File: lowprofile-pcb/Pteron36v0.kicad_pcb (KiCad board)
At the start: 2 copper layers, 123.5 x 95.6 mm, 47 parts, among them J1 AudioJack4, J2 AudioJack4, SW1 SW_PUSH, SW10 SW_PUSH, SW12 SW_PUSH, SW13 SW_PUSH, SW14 SW_PUSH, SW15 SW_PUSH, SW17 SW_PUSH, SW18 SW_PUSH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

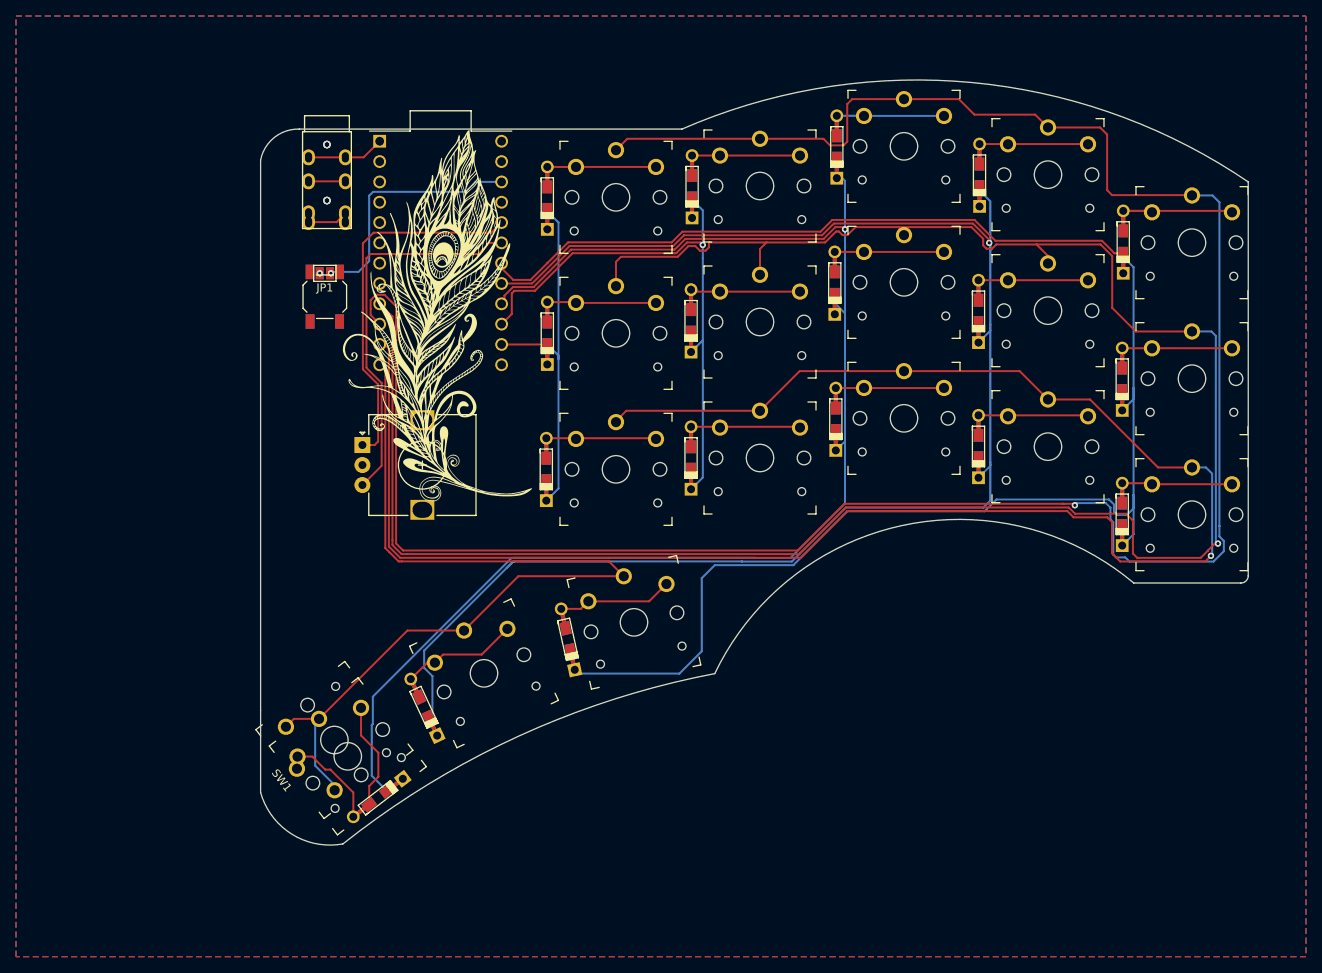
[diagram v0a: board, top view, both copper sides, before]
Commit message: add 4-th key in thumb for removable config
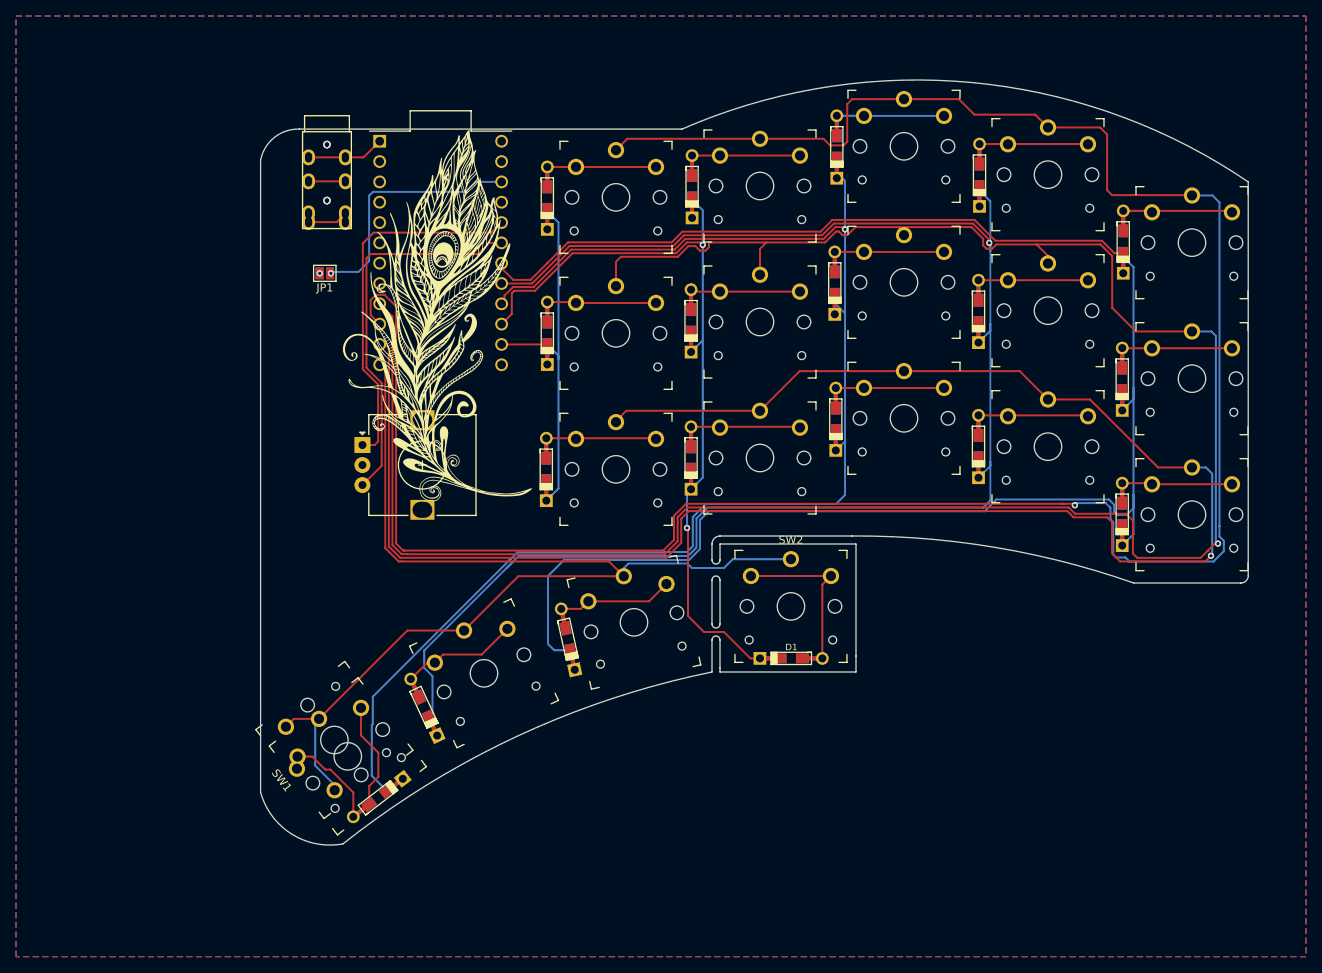
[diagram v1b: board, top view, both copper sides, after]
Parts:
- removed RST1, RST2: SW_PUSH, acheron_Hardware:smdPushBtn
- added D1: 1N4148, Keebio-Parts:Diode-dual, F.Cu at (183.9, 114.3)
- added SW2: SW_PUSH, keyswitches:PG1350_reversible, F.Cu at (183.9, 107.8)
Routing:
- net /Col4: track 71.5 -> 98.8 mm, vias 1 -> 2
- net /Row4: track 114.6 -> 137.4 mm
- net Net-(D1-Pad2): track 0.00 -> 20.7 mm
- net /Col1: track 211.9 -> 219.0 mm
- net /Col3: track 174.3 -> 176.5 mm
- net /Col2: track 200.5 -> 202.5 mm
- net /Row1: track 285.4 -> 287.1 mm
- net /Row3: track 229.9 -> 231.7 mm
- net /Row2: track 268.8 -> 270.5 mm
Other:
- outline, holes or cut-outs redrawn
